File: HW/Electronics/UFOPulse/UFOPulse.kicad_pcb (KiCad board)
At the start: 4 copper layers, 46 x 46 mm, 82 parts, among them J1 Conn_Coaxial, J10 Conn_01x02_Female, J2 Conn_Coaxial, J3 Conn_Coaxial, J4 Conn_Coaxial, J5 Conn_Coaxial, J6 Conn_Coaxial, J7 Conn_Coaxial, J8 Conn_Coaxial, J9 Conn_02x08_Odd_Even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

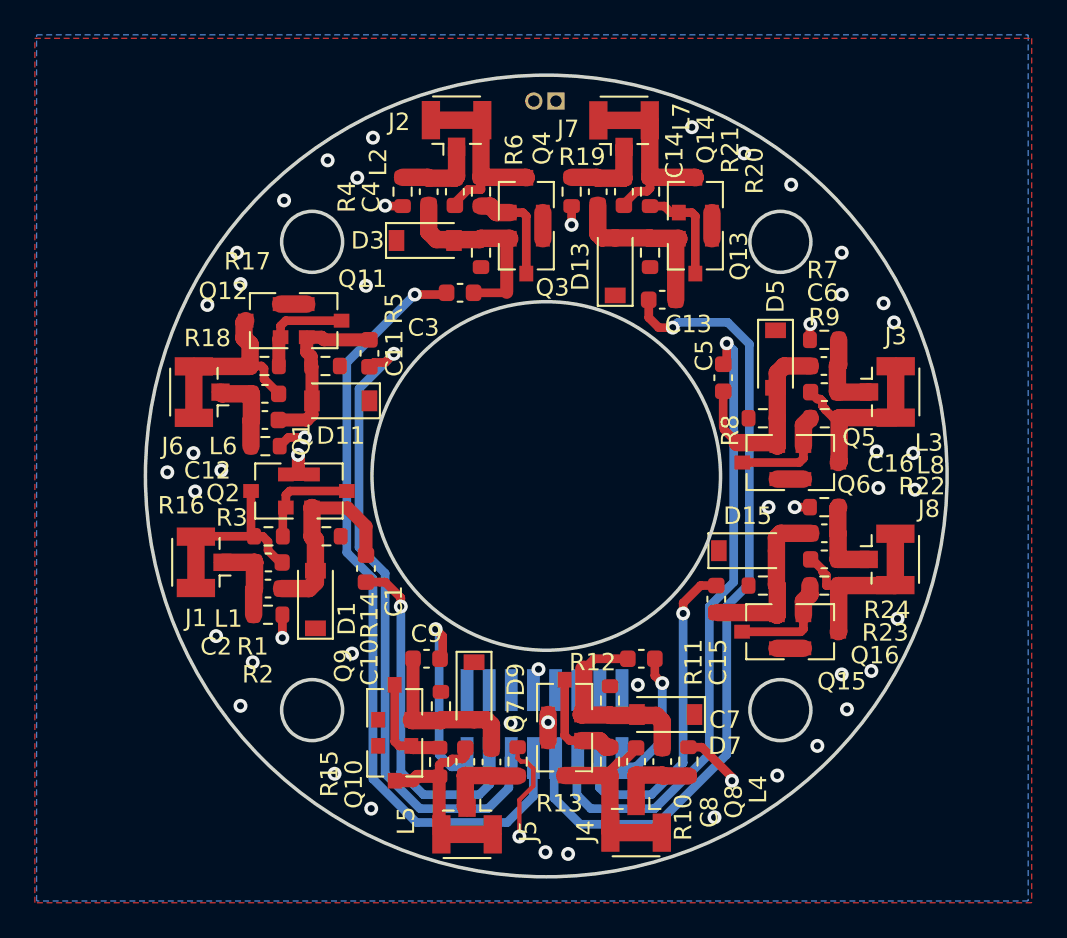
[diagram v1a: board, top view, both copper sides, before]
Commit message: files for manufactured mothership pulsedeck and controldeck
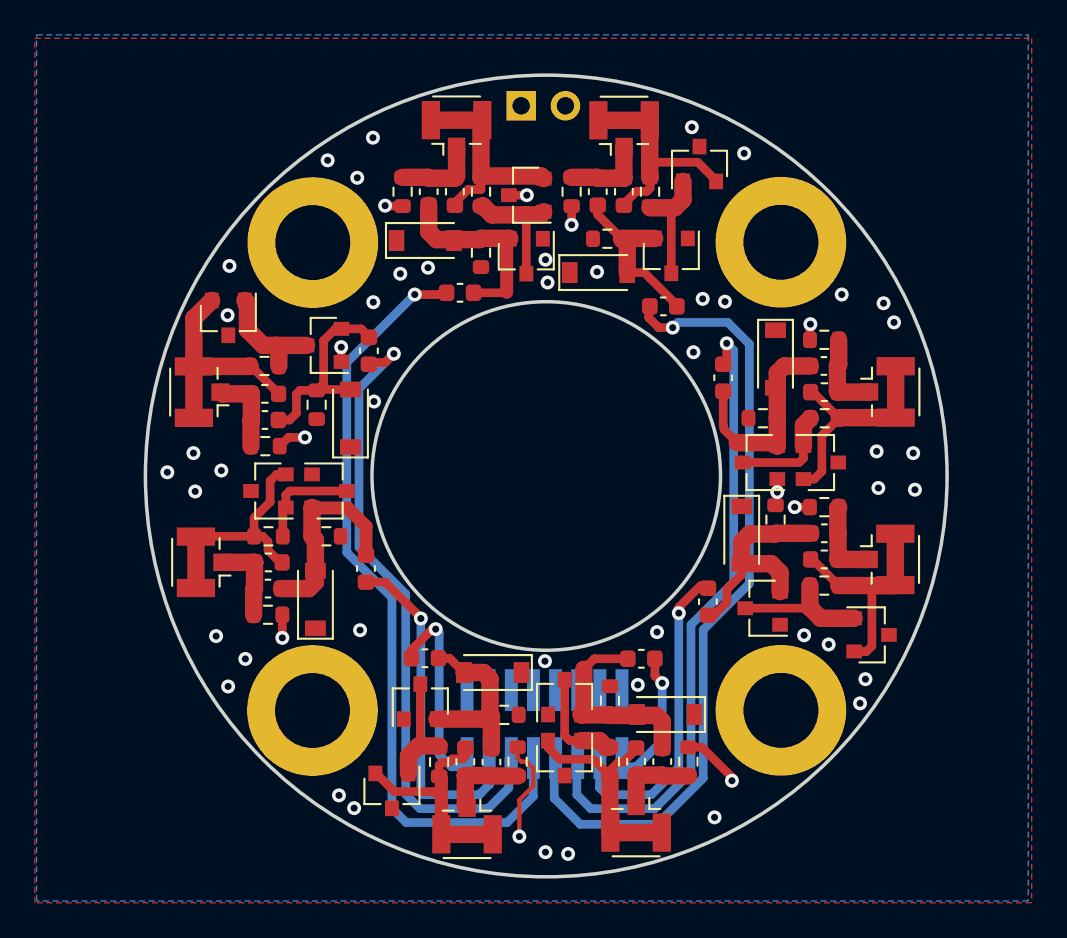
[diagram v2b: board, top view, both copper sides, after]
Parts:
- added H1: MountingHole, MountingHole:MountingHole_4.3mm_M4_DIN965_Pad, F.Cu at (127.2, 91.7)
- added H2: MountingHole, MountingHole:MountingHole_4.3mm_M4_DIN965_Pad, F.Cu at (154.0, 91.7)
- added H3: MountingHole, MountingHole:MountingHole_4.3mm_M4_DIN965_Pad, F.Cu at (154.0, 118.6)
- added H4: MountingHole, MountingHole:MountingHole_4.3mm_M4_DIN965_Pad, F.Cu at (127.1, 118.6)
- J10: footprint Connector_PinHeader_1.27mm:PinHeader_1x02_P1.27mm_Vertical -> Connector_PinHeader_2.54mm:PinHeader_1x02_P2.54mm_Vertical
- moved R23 3.85 mm to (153.7, 107.6), turned to 90 degrees
- moved R14 3.67 mm to (138.1, 118.8), turned to 0 degrees
- moved Q16 2.92 mm to (159.2, 114.2)
- moved R20 2.58 mm to (144.1, 91.5), turned to 180 degrees
- moved R17 2.28 mm to (127.4, 101.0), turned to -90 degrees
- moved J10 2.01 mm to (139.1, 83.9), turned to -90 degrees
- moved Q12 2.01 mm to (122.3, 96.0), turned to -90 degrees
- moved Q14 1.81 mm to (149.3, 87.2)
- moved Q10 1.59 mm to (131.7, 123.2)
- moved D9 1.51 mm to (137.5, 116.4), turned to 180 degrees
- moved Q9 1.47 mm to (133.3, 118.1)
- moved Q11 1.42 mm to (127.8, 97.6), turned to 180 degrees
- moved Q13 1.38 mm to (147.7, 92.5)
- moved Q15 1.36 mm to (153.0, 112.7)
- moved D11 1.15 mm to (129.3, 101.8), turned to 90 degrees
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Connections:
- Q10 pad 2: GND -> Net-(J5-Pad2)
- Q10 pad 3: Net-(J5-Pad2) -> GND
- Q12 pad 2: GND -> Net-(J6-Pad2)
- Q12 pad 3: Net-(J6-Pad2) -> GND
- Q14 pad 2: GND -> Net-(J7-Pad2)
- Q14 pad 3: Net-(J7-Pad2) -> GND
- Q16 pad 2: GND -> Net-(J8-Pad2)
- Q16 pad 3: Net-(J8-Pad2) -> GND
- Q2 pad 2: GND -> Net-(J1-Pad2)
- Q2 pad 3: Net-(J1-Pad2) -> GND
- Q4 pad 2: GND -> Net-(J2-Pad2)
- Q4 pad 3: Net-(J2-Pad2) -> GND
- Q6 pad 2: GND -> Net-(J3-Pad2)
- Q6 pad 3: Net-(J3-Pad2) -> GND
- Q8 pad 2: GND -> Net-(J4-Pad2)
- Q8 pad 3: Net-(J4-Pad2) -> GND
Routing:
- net GND: track 11.7 -> 1.89 mm, vias 44 -> 47
- net Net-(C15-Pad1): track 10.00 -> 12.9 mm
- net Net-(Q15-Pad3): track 6.24 -> 8.62 mm
- net Net-(J4-Pad2): track 11.2 -> 13.3 mm
- net Net-(J1-Pad2): track 11.6 -> 13.5 mm
- net Net-(J3-Pad2): track 11.2 -> 13.0 mm
- net Net-(J7-Pad2): track 11.4 -> 13.1 mm
- net Net-(J8-Pad2): track 11.5 -> 13.2 mm
- net Net-(J5-Pad2): track 11.8 -> 13.3 mm
- net Net-(C11-Pad1): track 10.3 -> 11.6 mm
- net Net-(J2-Pad2): track 11.5 -> 12.7 mm
- net Net-(Q3-Pad3): track 6.14 -> 7.26 mm
- net Net-(J6-Pad2): track 11.6 -> 12.7 mm
- net TRIG6: track 18.7 -> 17.7 mm
- net Net-(C10-Pad2): track 9.66 -> 10.6 mm
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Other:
- outline, holes or cut-outs redrawn
- net class Default removed
